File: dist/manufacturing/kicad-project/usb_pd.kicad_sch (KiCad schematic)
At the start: 74 parts, among them J1 USB4105-GF-A, Q1 BSS123LT1G, Q2 MMBT5551LT1G, Q3 MMBT5551LT1G, U1 TPD4S480RUKR, U2 TPS26750SRSMR, U3 M24512-RMN6TP, U4 SN74LVC1G08DBVR

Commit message: Complete orderable PD1180-EPR board release
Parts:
- removed GND (x20): GND, symbol Custom:rail_down
- removed PD_1V5 (x2): PD_1V5, symbol Custom:rail_up
- removed PD_3V3 (x9): PD_3V3, symbol Custom:rail_up
- removed Q1: BSS123LT1G, symbol Device:U_BSS123LT1G
- removed Q2, Q3: MMBT5551LT1G, symbol Device:U_MMBT5551LT1G
- removed USB_VBUS (x4): USB_VBUS, symbol Custom:rail_up
- removed V3V3 (x4): V3V3, symbol Custom:rail_up
- removed VBUS_LV (x2): VBUS_LV, symbol Custom:rail_up
- added C72: 100nF, symbol Device:capacitor_down
- added GND (x26): GND, symbol Custom:rail_down
- added J10: USB4105-GF-A, symbol Device:J_USB4105-GF-A
- added PD_1V5 (x2): PD_1V5, symbol Custom:rail_up
- added PD_3V3 (x9): PD_3V3, symbol Custom:rail_up
- added Q1: Q1, symbol Custom:BSS123LT1G_NMOS
- added Q2: Q2, symbol Custom:MMBT5551LT1G_NPN
- added Q3: Q3, symbol Custom:MMBT5551LT1G_NPN
- added R105, R106: 5.1kΩ, symbol Device:boxresistor_down
- added R107, R108: 100kΩ, symbol Device:boxresistor_down
- added USB_DATA_VBUS: USB_DATA_VBUS, symbol Custom:rail_up
- added USB_VBUS (x3): USB_VBUS, symbol Custom:rail_up
- added V3V3 (x5): V3V3, symbol Custom:rail_up
- added VBUS_LV (x2): VBUS_LV, symbol Custom:rail_up
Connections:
- net PD_PATH_N is gone; now on an unnamed net: R11.2
- net at C10.1: now also V3V3.1; no longer U4.5 (VCC)
- net at C10.2: now also U4.3 (GND), GND.1
- net at R10.2: now also GND.1, Q2.2 (emitter)
- net at R14.2: now also R15.2, GND.1
- net at C3.2, C4.2: now also GND.1; no longer C5.2
- net at U3.7 (N_WC): now also GND.1
- net at C5.1: now also VBUS_LV.1
- net at C9.2: now also GND.1
- net at R2.2: now also GND.1
- net at R6.1, R7.1: now also PD_3V3.1
- net at U1.10 (VPWR): now also PD_3V3.1
- net at U1.13 (GND2), U1.8 (GND3): now also GND.1
- net at U1.18 (GND1), U1.21 (EP): now also GND.1
- net at U1.20 (VBUS): now also USB_VBUS.1
- net at R4.1: now also R3.1, PD_3V3.1
- net at U2.11 (GND1), U2.12 (GND2), U2.13 (GPIO11)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: now also GND.1
- net at C6.1: now also R13.1, V3V3.1; no longer R11.1
- net at C7.1: now also PD_3V3.1
- net at U2.3 (ADCIN2), U2.6 (GPIO1): now also GND.1
- net at U3.1 (E0), U3.2 (E1), U3.3 (E2)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: now also GND.1
- net at R5.1, U3.8 (VCC): now also PD_3V3.1
- net at U2.18 (GPIO3), U2.19 (GND5), U2.22 (GPIO4)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: now also GND.1
- net at C2.1: now also PD_3V3.1
- net at J1.7 (VBUS1), J1.8 (VBUS2): now also USB_VBUS.1
- net at C9.1: now also PD_3V3.1; no longer R3.1
- net at R13.2: now also Q3.3 (collector)
- net at U2.4 (LDO_1V5): now also PD_1V5.1
- net at R8.1: now also PD_3V3.1
- net at U2.30 (GPIO7), U2.31 (GPIO6), U2.33 (GND4): now also GND.1
- net at C8.1: now also PD_1V5.1
- net at C1.2, C2.2: now also GND.1
- net at R1.1: now also PD_3V3.1
- net at U2.32 (VIN_3V3): now also V3V3.1
- net PD_IRQ_N: now reaches R8.2
- removed net GND: J1.19 (GND3), J1.20 (GND4)
- new net: GND.1, R108.2
- new net: GND.1, J10.5 (GND1), J10.6 (GND2)
- new net: J10.7 (VBUS1), J10.8 (VBUS2), R107.1
- new net: R11.1, V3V3.1
- new net: GND.1, Q3.2 (emitter)
- new net: C7.2, GND.1
- new net: C8.2, GND.1
- new net: GND.1, R105.2
- new net: C6.2, GND.1
- new net: Q1.2 (source), VBUS_LV.1
- new net: Q1.3 (drain), USB_VBUS.1
- new net: C72.2, GND.1
- new net: GND.1, R106.2
- new net: GND.1, J1.5 (GND1), J1.6 (GND2)
- new net: C5.2, GND.1
- new net: U4.5 (VCC), V3V3.1
- new net USB_DATA_VBUS_SENSE: R108.1
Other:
- note added: "01 / USB-C EPR Power and USB Data"
- note added: "J1 is 48 V / 5 A EPR power; J10 is isolated USB 2.0 device data and 5 V attach sense."
- note added: "Q1: protected VBUS blocking control. Q2/Q3: PD path level translation and valid-path indication."
- note added: "U1: 48 V CC/VBUS protection. U2: TPS26750 EPR sink controller. U3: PD policy EEPROM. U4: hardware power-permit gate."
- note added: "USB_DATA_CC1"
- note added: "USB_DATA_CC2"
- note added: "USB_DATA_VBUS_SENSE"
- note removed: "01 / USB-C EPR and USB Data"
- note removed: "48 V / 5 A EPR sink target; EEPROM requires TI configuration image."

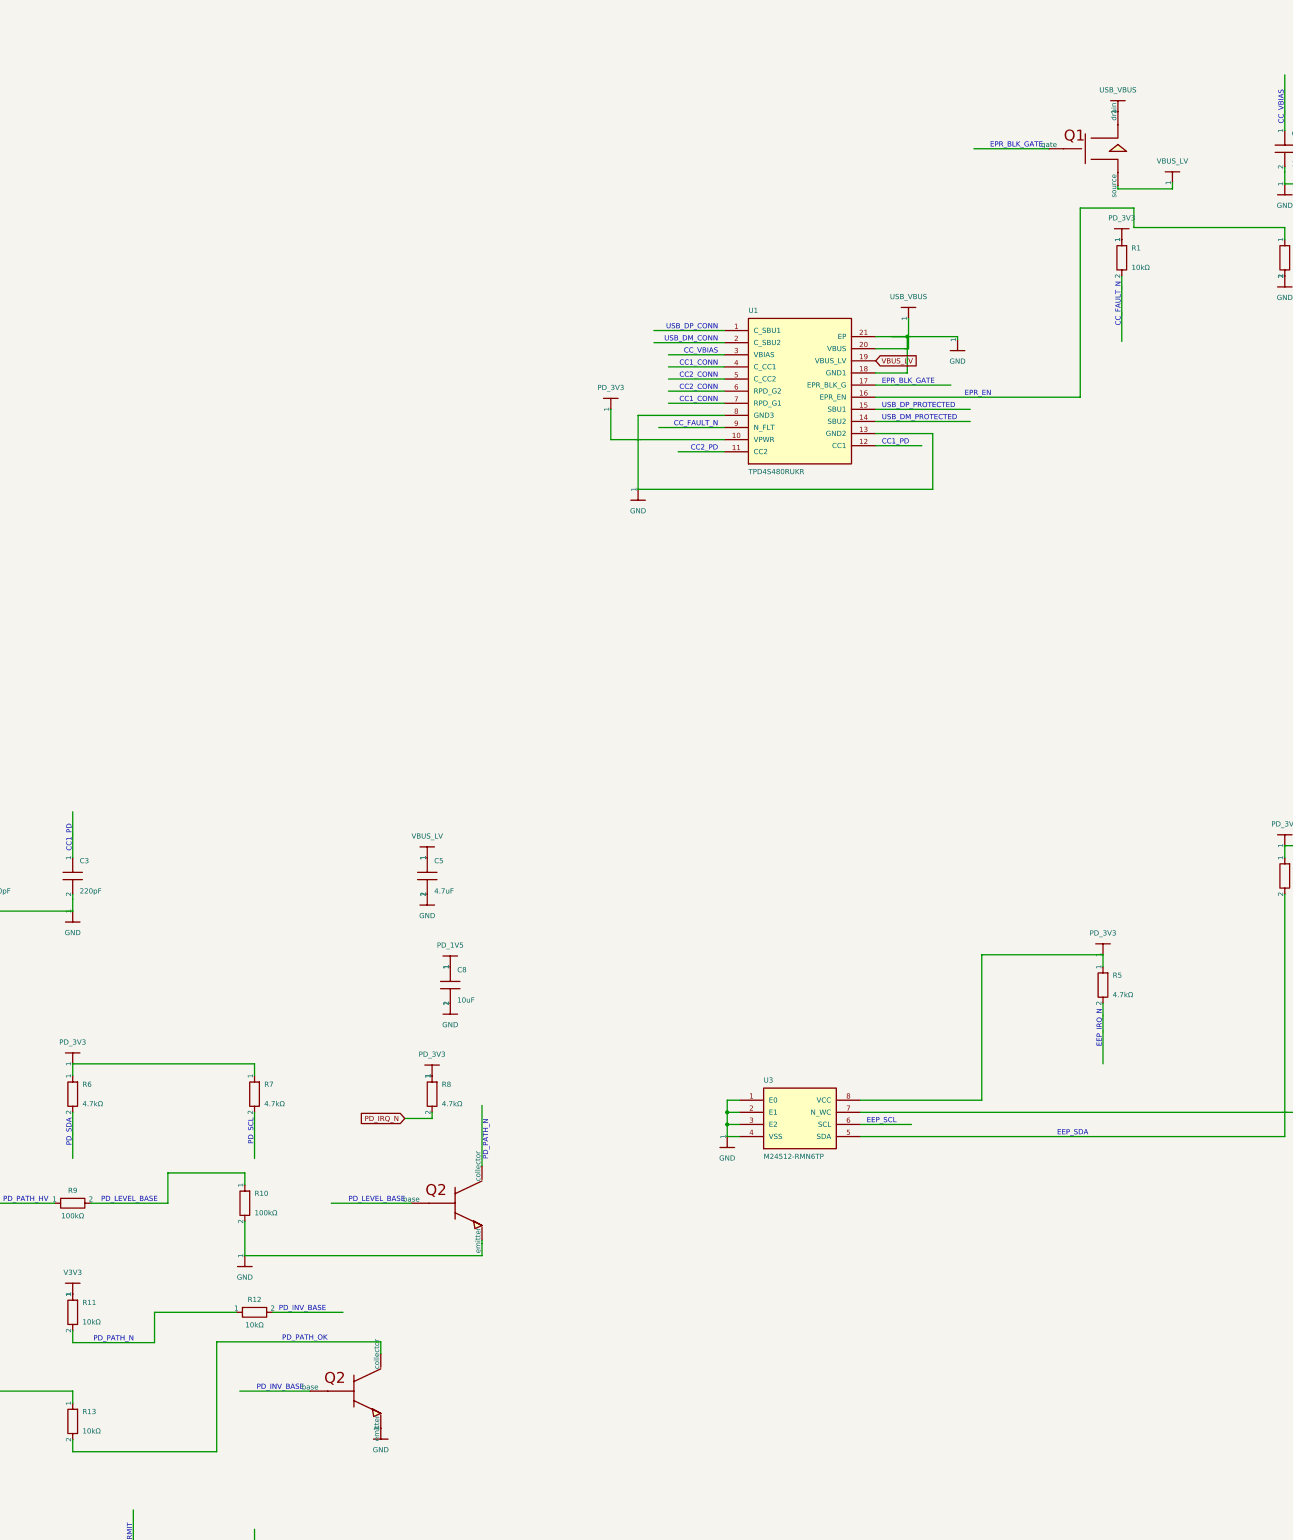
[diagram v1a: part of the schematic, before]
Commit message: Fix schematic style and top-side reset switch
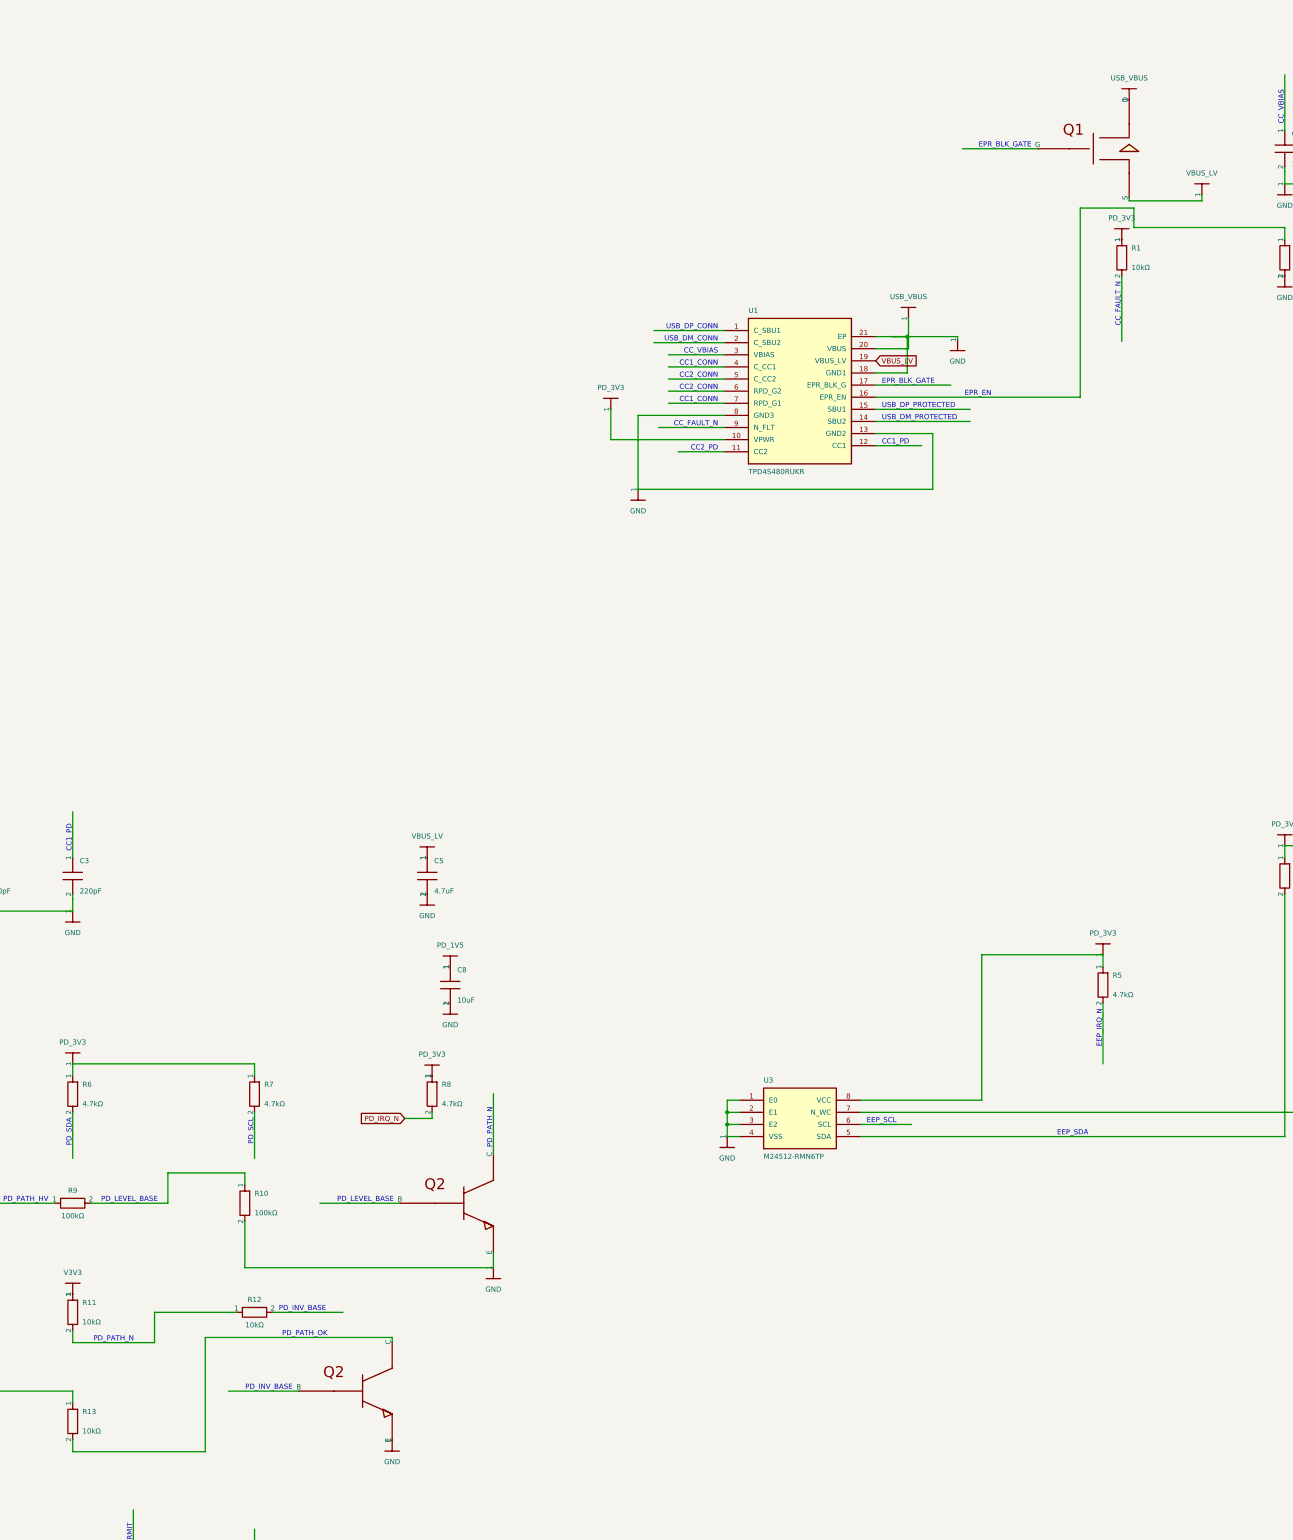
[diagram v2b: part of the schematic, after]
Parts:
- removed GND (x26): GND, symbol Custom:rail_down
- removed PD_1V5 (x2): PD_1V5, symbol Custom:rail_up
- removed PD_3V3 (x9): PD_3V3, symbol Custom:rail_up
- removed USB_VBUS (x3): USB_VBUS, symbol Custom:rail_up
- removed V3V3 (x5): V3V3, symbol Custom:rail_up
- removed VBUS_LV (x2): VBUS_LV, symbol Custom:rail_up
- added GND (x26): GND, symbol Custom:rail_down
- added PD_1V5 (x2): PD_1V5, symbol Custom:rail_up
- added PD_3V3 (x9): PD_3V3, symbol Custom:rail_up
- added USB_VBUS (x3): USB_VBUS, symbol Custom:rail_up
- added V3V3 (x5): V3V3, symbol Custom:rail_up
- added VBUS_LV (x2): VBUS_LV, symbol Custom:rail_up
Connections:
- net at U2.3 (ADCIN2), U2.6 (GPIO1): now also GND.1
- net at R108.2: now also GND.1
- net at R2.2: now also GND.1
- net at J10.5 (GND1), J10.6 (GND2): now also GND.1
- net at U2.32 (VIN_3V3): now also V3V3.1
- net at U2.4 (LDO_1V5): now also PD_1V5.1
- net at U2.11 (GND1), U2.12 (GND2), U2.13 (GPIO11)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: now also GND.1
- net at U2.18 (GPIO3), U2.19 (GND5), U2.22 (GPIO4)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: now also GND.1
- net at U2.30 (GPIO7), U2.31 (GPIO6), U2.33 (GND4): now also GND.1
- net at C6.1, R13.1: now also V3V3.1
- net at R11.1: now also V3V3.1
- net at R5.1, U3.8 (VCC): now also PD_3V3.1
- net at R8.1: now also PD_3V3.1
- net at Q3.2 (E): now also GND.1
- net at C7.2: now also GND.1
- net at C8.2: now also GND.1
- net at R1.1: now also PD_3V3.1
- net at R105.2: now also GND.1
- net at Q2.2 (E), R10.2: now also GND.1
- net at R14.2, R15.2: now also GND.1
- net at C10.1: now also V3V3.1
- net at C3.2, C4.2: now also GND.1
- net at C6.2: now also GND.1
- net at Q1.2 (S): now also VBUS_LV.1
- net at Q1.3 (D): now also USB_VBUS.1
- net at R3.1, R4.1: now also PD_3V3.1
- net at C9.1: now also PD_3V3.1
- net at C9.2: now also GND.1
- net at U1.10 (VPWR): now also PD_3V3.1
- net at U1.13 (GND2), U1.8 (GND3): now also GND.1
- net at U1.18 (GND1), U1.21 (EP): now also GND.1
- net at U1.20 (VBUS): now also USB_VBUS.1
- net at R6.1, R7.1: now also PD_3V3.1
- net at U3.1 (E0), U3.2 (E1), U3.3 (E2)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: now also GND.1
- net at U3.7 (N_WC): now also GND.1
- net at C5.1: now also VBUS_LV.1
- net at C7.1: now also PD_3V3.1
- net at C72.2: now also GND.1
- net at R106.2: now also GND.1
- net at J1.7 (VBUS1), J1.8 (VBUS2): now also USB_VBUS.1
- net at C8.1: now also PD_1V5.1
- net at J1.5 (GND1), J1.6 (GND2): now also GND.1
- net at C1.2, C2.2: now also GND.1
- net at C2.1: now also PD_3V3.1
- net at C5.2: now also GND.1
- net at U4.5 (VCC): now also V3V3.1
- net at C10.2, U4.3 (GND): now also GND.1

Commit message: Use one USB-C port for PD and data
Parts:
- removed GND (x26): GND, symbol Custom:rail_down
- removed J10: USB4105-GF-A, symbol Device:J_USB4105-GF-A
- removed PD_1V5 (x2): PD_1V5, symbol Custom:rail_up
- removed PD_3V3 (x9): PD_3V3, symbol Custom:rail_up
- removed R105, R106: 5.1kΩ, symbol Device:boxresistor_down
- removed USB_DATA_VBUS: USB_DATA_VBUS, symbol Custom:rail_up
- removed USB_VBUS (x3): USB_VBUS, symbol Custom:rail_up
- removed V3V3 (x5): V3V3, symbol Custom:rail_up
- removed VBUS_LV (x2): VBUS_LV, symbol Custom:rail_up
- added GND (x23): GND, symbol Custom:rail_down
- added PD_1V5 (x2): PD_1V5, symbol Custom:rail_up
- added PD_3V3 (x9): PD_3V3, symbol Custom:rail_up
- added USB_VBUS (x4): USB_VBUS, symbol Custom:rail_up
- added V3V3 (x5): V3V3, symbol Custom:rail_up
- added VBUS_LV (x2): VBUS_LV, symbol Custom:rail_up
- R107: value 100kΩ -> 1MΩ
- R108: value 100kΩ -> 47kΩ
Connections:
- net at R8.1: now also PD_3V3.1
- net at R108.2: now also GND.1
- net at C5.1: now also VBUS_LV.1
- net at C5.2: now also GND.1
- net at R1.1: now also PD_3V3.1
- net at R107.1: now also USB_VBUS.1
- net at U2.30 (GPIO7), U2.31 (GPIO6), U2.33 (GND4): now also GND.1
- net at C9.2: now also GND.1
- net at C1.2, C2.2: now also GND.1
- net at U2.3 (ADCIN2), U2.6 (GPIO1): now also GND.1
- net at C2.1: now also PD_3V3.1
- net at R11.1: now also V3V3.1
- net at U2.11 (GND1), U2.12 (GND2), U2.13 (GPIO11)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: now also GND.1
- net at C8.1: now also PD_1V5.1
- net at U4.5 (VCC): now also V3V3.1
- net at U1.13 (GND2), U1.8 (GND3): now also GND.1
- net at U2.4 (LDO_1V5): now also PD_1V5.1
- net at Q2.2 (E), R10.2: now also GND.1
- net at R14.2, R15.2: now also GND.1
- net at J1.7 (VBUS1), J1.8 (VBUS2): now also USB_VBUS.1
- net at R3.1, R4.1: now also PD_3V3.1
- net at C8.2: now also GND.1
- net at C9.1: now also PD_3V3.1
- net at C6.1, R13.1: now also V3V3.1
- net at U3.7 (N_WC): now also GND.1
- net at C10.1: now also V3V3.1
- net at C10.2, U4.3 (GND): now also GND.1
- net at C72.2: now also GND.1
- net at R5.1, U3.8 (VCC): now also PD_3V3.1
- net at C7.1: now also PD_3V3.1
- net at C3.2, C4.2: now also GND.1
- net at J1.5 (GND1), J1.6 (GND2): now also GND.1
- net at Q3.2 (E): now also GND.1
- net at U1.10 (VPWR): now also PD_3V3.1
- net at U1.18 (GND1), U1.21 (EP): now also GND.1
- net at U1.20 (VBUS): now also USB_VBUS.1
- net at R6.1, R7.1: now also PD_3V3.1
- net at C6.2: now also GND.1
- net at Q1.2 (S): now also VBUS_LV.1
- net at Q1.3 (D): now also USB_VBUS.1
- net at R2.2: now also GND.1
- net at U3.1 (E0), U3.2 (E1), U3.3 (E2)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: now also GND.1
- net at U2.18 (GPIO3), U2.19 (GND5), U2.22 (GPIO4)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: now also GND.1
- net at U2.32 (VIN_3V3): now also V3V3.1
- net at C7.2: now also GND.1
- net USB_DATA_VBUS_SENSE: no longer names the net of R108.1
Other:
- note added: "J1 carries 48 V / 5 A EPR power and USB 2.0 device data on one USB-C receptacle."
- note added: "R107/R108/C72: 5-60 V attach sense. Q1: protected VBUS control. Q2/Q3: PD-path level translation."
- note added: "U1: 48 V CC/VBUS and D+/D- protection. U2: TPS26750 EPR sink controller. U3: PD policy EEPROM. U4: hardware power-permit gate."
- note added: "USB_VBUS_SENSE"
- note removed: "J1 is 48 V / 5 A EPR power; J10 is isolated USB 2.0 device data and 5 V attach sense."
- note removed: "Q1: protected VBUS blocking control. Q2/Q3: PD path level translation and valid-path indication."
- note removed: "U1: 48 V CC/VBUS protection. U2: TPS26750 EPR sink controller. U3: PD policy EEPROM. U4: hardware power-permit gate."
- note removed: "USB_DATA_CC1"
- note removed: "USB_DATA_CC2"
- note removed: "USB_DATA_VBUS_SENSE"

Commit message: fix: finalize single-port EPR controller
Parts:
- removed GND (x23): GND, symbol Custom:rail_down
- removed PD_1V5 (x2): PD_1V5, symbol Custom:rail_up
- removed PD_3V3 (x9): PD_3V3, symbol Custom:rail_up
- removed Q2: Q2, symbol Custom:MMBT5551LT1G_NPN
- removed Q3: Q3, symbol Custom:MMBT5551LT1G_NPN
- removed R10: 100kΩ, symbol Device:boxresistor_down
- removed USB_VBUS (x4): USB_VBUS, symbol Custom:rail_up
- removed V3V3 (x5): V3V3, symbol Custom:rail_up
- removed VBUS_LV (x2): VBUS_LV, symbol Custom:rail_up
- added Q2: Q2, CSD17484F4, symbol Custom:CSD17484F4_NMOS
- added Q3: Q3, CSD17484F4, symbol Custom:CSD17484F4_NMOS
- C1, C10, C3, C4, C6, C7, C72, C8, C9: footprint (none) -> capacitor_cap0603
- C2: value 100nF -> 1uF; footprint (none) -> capacitor_cap0603
- C5: footprint (none) -> capacitor_cap1206
- J1: value USB4105-GF-A -> J1; footprint (none) -> USB4105-GF-A
- Q1: footprint (none) -> BSS123LT1G
- R1, R107, R108, R14, R15, R2, R3, R4, R5, R6, R7, R8: footprint (none) -> resistor_res0603
- R11, R13: value 10kΩ -> 100kΩ; footprint (none) -> resistor_res0603
- R12: value 10kΩ -> 0Ω; footprint (none) -> resistor_res0603
- R9: value 100kΩ -> 0Ω; footprint (none) -> resistor_res0603
- U1: footprint (none) -> TPD4S480RUKR
- U2: footprint (none) -> TPS26750SRSMR
- U3: footprint (none) -> M24512-RMN6TP
- U4: footprint (none) -> SN74LVC1G08DBVR
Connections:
- net PD_IRQ_N: now also U2.10 (N_I2Ct_IRQ)
- net VBUS_LV: now also C5.1, Q1.2 (S), U2.26 (VBUS1), U2.27 (VBUS2)
- net PD_3V3: now reaches R8.1
- net PD_3V3: now also C2.1, C7.1, C9.1, R1.1, R11.1, R13.1, R3.1, R4.1, R5.1, R6.1, R7.1, U1.10 (VPWR), U2.1 (LDO_3V3), U2.2 (ADCIN1), U3.8 (VCC)
- net PD_PATH_N: now reaches R11.2, R12.1
- net PD_PATH_N: now also Q2.3 (D)
- net PD_INV_BASE: now reaches R12.2
- net PD_INV_BASE: now also Q3.1 (G)
- net V3V3: now reaches C6.1
- net V3V3: now also C10.1, U2.32 (VIN_3V3), U4.5 (VCC); no longer R13.1
- net GND: now reaches C6.2
- net GND: now also C1.2, C10.2, C2.2, C3.2, C4.2, C5.2, C7.2, C72.2, C8.2, C9.2, J1.1 (EH1), J1.19 (GND1), J1.2 (GND1), J1.20 (GND1), J1.3 (GND1), J1.4 (GND1), J1.5 (GND1), J1.6 (GND1), R108.2, R14.2, R15.2, R2.2, U1.13 (GND2), U1.18 (GND1), U1.21 (EP), U1.8 (GND3), U2.11 (GND1), U2.12 (GND2), U2.13 (GPIO11), U2.14 (GND3), U2.18 (GPIO3), U2.19 (VSYS), U2.22 (GPIO4), U2.23 (GPIO5), U2.3 (ADCIN2), U2.30 (GPIO7), U2.31 (GPIO6), U2.33 (GND4), U2.6 (GPIO1), U3.1 (E0), U3.2 (E1), U3.3 (E2), U3.4 (VSS), U3.7 (WC), U4.3 (GND), Q2.2 (S), Q3.2 (S)
- net USB_DP_CONN: now reaches J1.11 (DP)
- net USB_DP_CONN: now also J1.13 (DP), U1.1 (DP)
- net CC1_CONN: now reaches J1.15 (CC1)
- net CC1_CONN: now also U1.4 (CC1), U1.7 (CC1)
- net USB_VBUS: now reaches J1.7 (VBUS), J1.8 (VBUS)
- net USB_VBUS: now also J1.17 (VBUS), J1.18 (VBUS), Q1.3 (D), R107.1, U1.20 (VBUS)
- net CC2_CONN: now reaches J1.9 (CC2)
- net CC2_CONN: now also U1.5 (CC2), U1.6 (CC2)
- net CC_VBIAS: now reaches C1.1
- net CC_VBIAS: now also U1.3 (VBIAS)
- net EPR_BLK_GATE: now reaches Q1.1 (G)
- net EPR_BLK_GATE: now also U1.17 (EPR_BLK_G)
- net USB_VBUS_SENSE: now reaches C72.1
- net USB_VBUS_SENSE: now also R107.2, R108.1
- net CC1_PD: now reaches C3.1
- net CC1_PD: now also U1.12 (CC1), U2.24 (CC1)
- net PD_PATH_OK: now reaches R13.2
- net PD_PATH_OK: now also U4.1 (A), Q3.3 (D)
- net PD_LEVEL_BASE: now reaches R9.2
- net PD_LEVEL_BASE: now also Q2.1 (G)
- net EFUSE_EN: now reaches R15.1
- net EFUSE_EN: now also U4.4 (Y)
- net EEP_SDA: now reaches R3.2, U3.5 (SDA)
- net EEP_SDA: now also U2.15 (I2Cc_SDA)
- net EEP_SCL: now reaches U3.6 (SCL)
- net EEP_SCL: now also R4.2, U2.16 (I2Cc_SCL)
- net POWER_PERMIT: now reaches U4.2 (B)
- net POWER_PERMIT: now also R14.1
- net PD_1V5: now reaches C8.1
- net PD_1V5: now also U2.4 (LDO_1V5)
- net CC2_PD: now reaches C4.1, U2.25 (CC2)
- net CC2_PD: now also U1.11 (CC2)
- net PD_SDA: now reaches R6.2
- net PD_SDA: now also U2.8 (I2Ct_SDA)
- net EPR_EN: now reaches R2.1, U1.16 (EPR_EN)
- net EPR_EN: now also U2.7 (GPIO2)
- net PD_PATH_HV: now reaches R9.1
- net PD_PATH_HV: now also U2.20 (POWER_PATH_EN)
- net EEP_IRQ_N: now reaches R5.2
- net EEP_IRQ_N: now also U2.17 (N_I2Cc_IRQ)
- net CC_FAULT_N: now reaches U2.5 (GPIO0)
- net CC_FAULT_N: now also R1.2, U1.9 (N_FLT)
- net PD_SCL: now reaches U2.9 (I2Ct_SCL)
- net PD_SCL: now also R7.2
- net USB_DM_PROTECTED: now reaches U1.14 (SBU2)
- net USB_DP_PROTECTED: now reaches U1.15 (SBU1)
- net USB_DM_CONN: now reaches U1.2 (DM)
- net USB_DM_CONN: now also J1.12 (DM), J1.14 (DM)
- no-connect marks 0 -> 5
